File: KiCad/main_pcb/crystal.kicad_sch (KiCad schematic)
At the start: 3 parts, among them Y1 Crystal_GND24

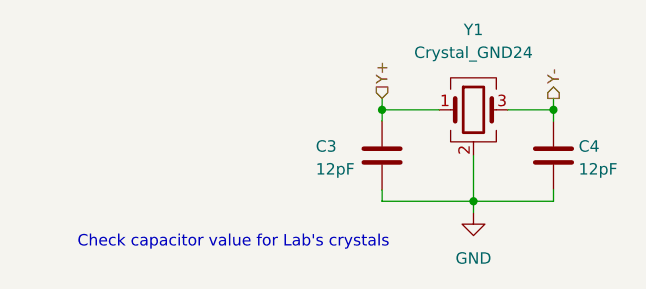
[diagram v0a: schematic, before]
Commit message: chore(migration): Migrates to homebrew symbols for PCB.
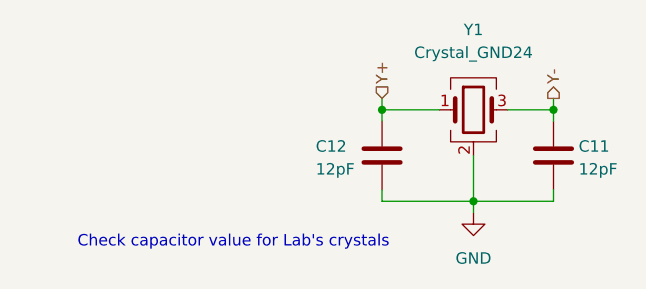
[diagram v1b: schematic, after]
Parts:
- Y1: private KLC_S4.1 -> (none)
- renumbered C4 to C11, C3 to C12
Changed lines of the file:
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@@
 		(on_board yes)
 		(dnp no)
-		(property "Reference" "C3"
+		(property "Reference" "C12"
 			(at 103.124 92.964 0)
 			(effects
@@
 			(project "main_pcb"
 				(path "/ecf3cf27-e370-4cc5-86a4-628206277f58/4c1a0284-1742-4ed4-9190-6f37324df6a7"
-					(reference "C3")
+					(reference "C12")
 					(unit 1)
 				)
@@
 		(on_board yes)
 		(dnp no)
-		(property "Reference" "C4"
+		(property "Reference" "C11"
 			(at 132.334 92.964 0)
 			(effects
@@
 			(project "main_pcb"
 				(path "/ecf3cf27-e370-4cc5-86a4-628206277f58/4c1a0284-1742-4ed4-9190-6f37324df6a7"
-					(reference "C4")
+					(reference "C11")
 					(unit 1)
 				)
@@
 			(effects
 				(font
-					(size 1.27 1.27)
-				)
-				(hide yes)
-			)
-		)
-		(property private "KLC_S3.3" "The rectangle is not a symbol body but a graphical element"
-			(at 120.65 101.6 0)
-			(show_name yes)
-			(effects
-				(font
-					(size 1.27 1.27)
-				)
-				(hide yes)
-			)
-		)
-		(property private "KLC_S4.1" "Some pins are on 50mil grid to make the symbol small"
-			(at 120.65 104.14 0)
-			(show_name yes)
-			(effects
-				(font

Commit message: feat(pcb): I think that's about right
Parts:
- C11, C12: footprint Capacitor_SMD:C_0603_1608Metric_Pad1.08x0.95mm_HandSolder -> Lilibrary:Capacitor_0603
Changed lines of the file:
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@@
 			)
 		)
-		(property "Footprint" "Capacitor_SMD:C_0603_1608Metric_Pad1.08x0.95mm_HandSolder"
+		(property "Footprint" "Lilibrary:Capacitor_0603"
 			(at 109.5248 90.17 0)
 			(effects
@@
 			)
 		)
-		(property "Footprint" "Capacitor_SMD:C_0603_1608Metric_Pad1.08x0.95mm_HandSolder"
+		(property "Footprint" "Lilibrary:Capacitor_0603"
 			(at 128.5748 90.17 0)
 			(effects

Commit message: feat(3D models): Adds 3D models to PCB
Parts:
- Y1: footprint Crystal:Crystal_SMD_3225-4Pin_3.2x2.5mm_HandSoldering -> Lilibrary:Crystal_3225
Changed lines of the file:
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@@
 			)
 		)
-		(property "Footprint" "Crystal:Crystal_SMD_3225-4Pin_3.2x2.5mm_HandSoldering"
+		(property "Footprint" "Lilibrary:Crystal_3225"
 			(at 120.65 88.9 0)
 			(effects
